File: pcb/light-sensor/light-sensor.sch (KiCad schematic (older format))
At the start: 13 parts, among them J1 HEADER-1x04, J2 HEADER-1x01, Q1 BSS138, Q2 BSS138, U1 LP2981, U2 TSL2561

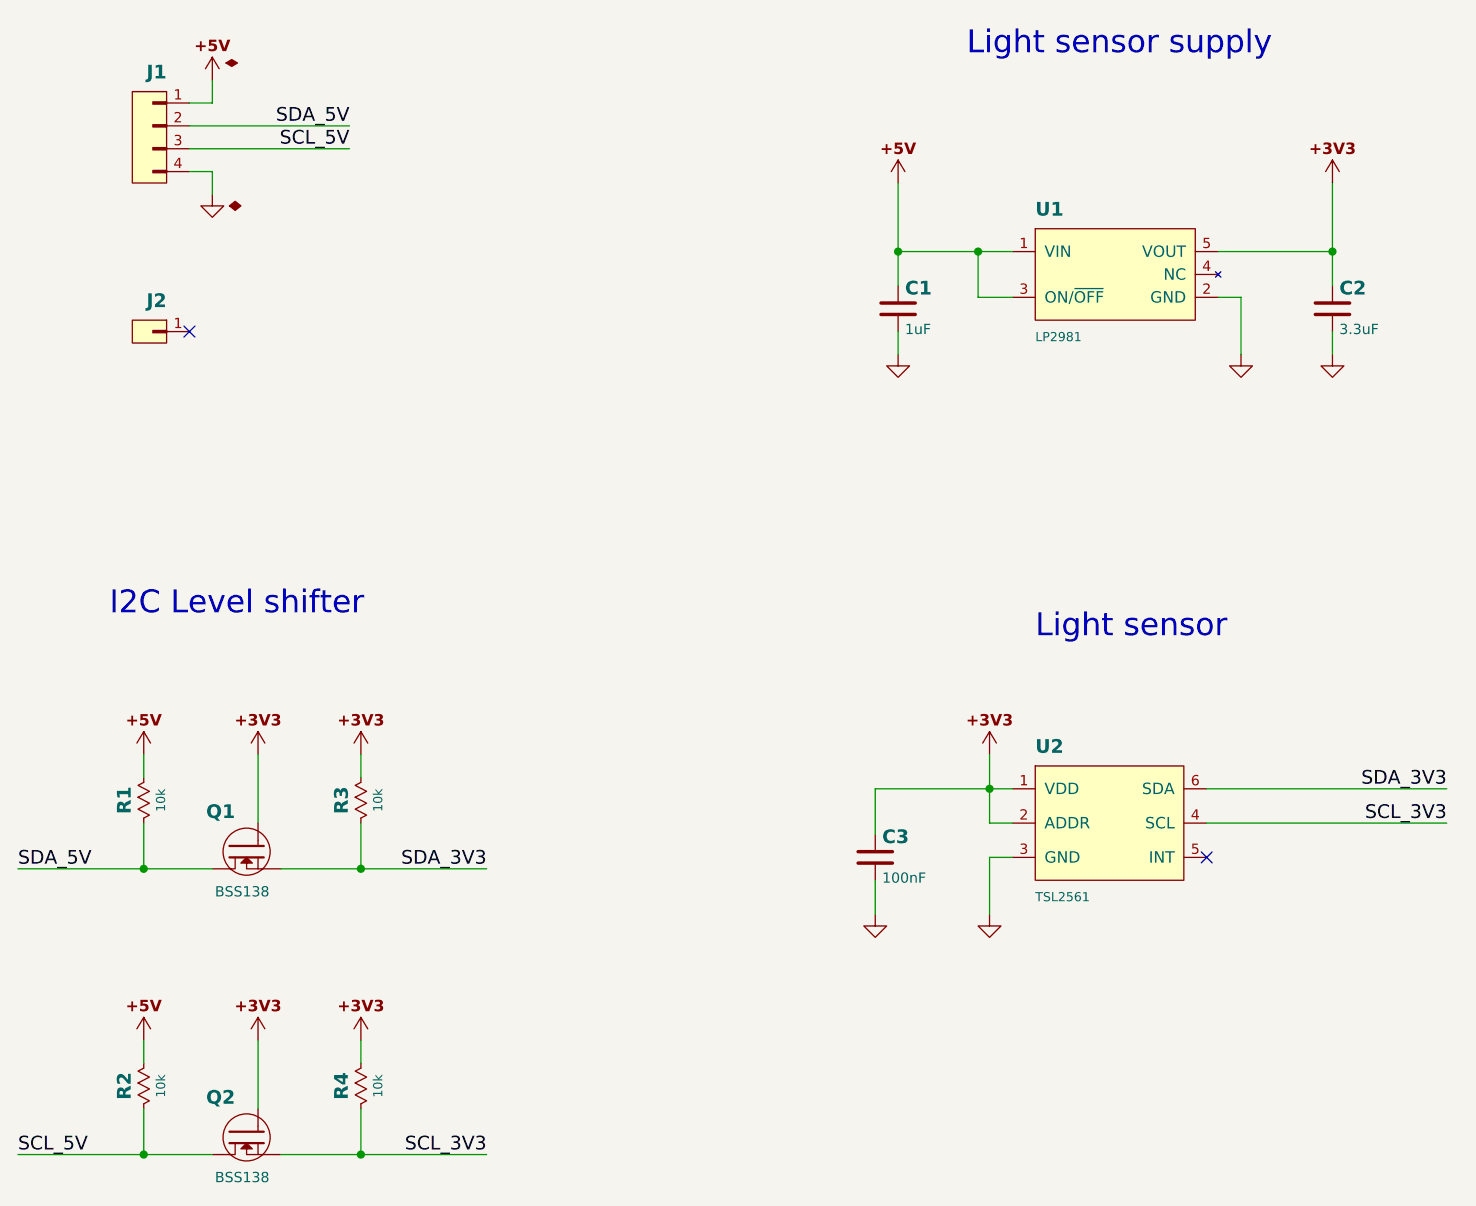
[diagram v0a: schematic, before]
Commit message: Removed 3.3v regulator and level shifters
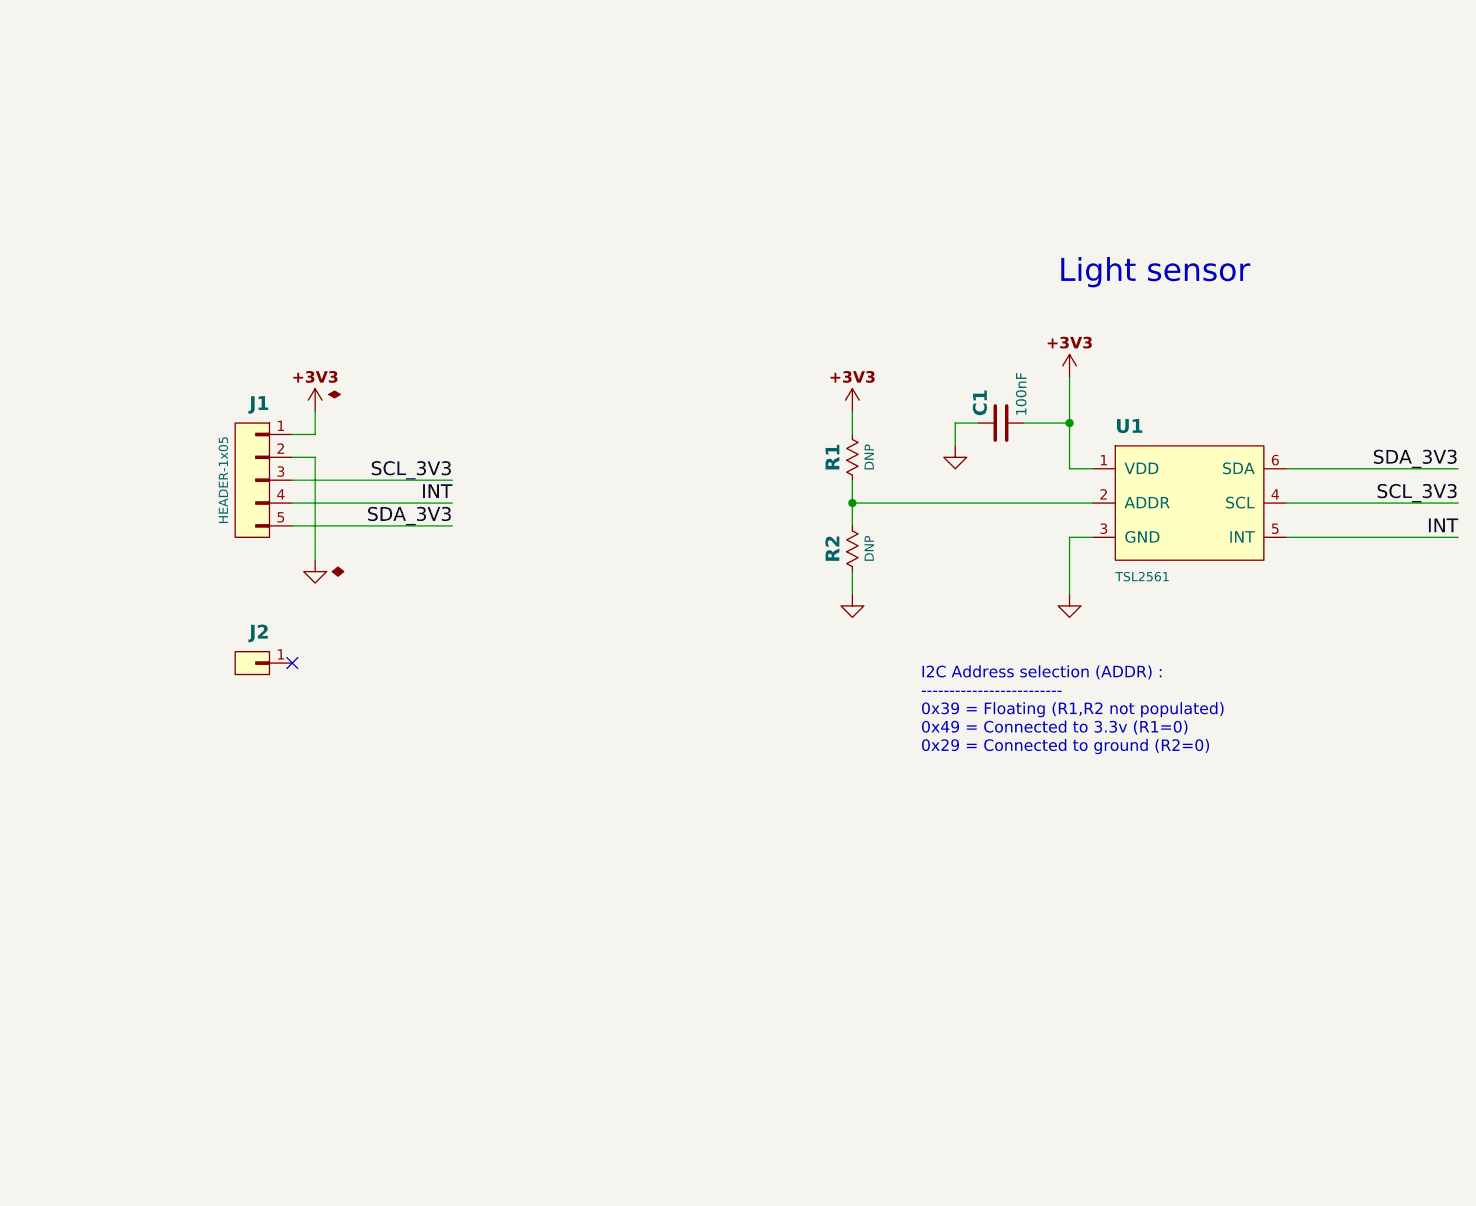
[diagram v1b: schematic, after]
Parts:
- removed C1: 1uF, SMT:C-0805, symbol CAP
- removed C2: 3.3uF, SMT:C-0805, symbol CAP
- removed J1: HEADER-1x04, Conn-Wire-Pads:WP-50mil-1x04, symbol HEADER-1x04
- removed Q1, Q2: BSS138, SMT-SOT:SOT23, symbol N-MOSFET
- removed R3, R4: 10k, SMT:R-0603, symbol RESISTOR
- removed U1: LP2981, SMT-SOT:SOT23-5, symbol LP2981
- added J1: HEADER-1x05, Conn-Wire-Pads:WP-40mil-1x05, symbol HEADER-1x05
- J2: footprint Conn-Wire-Pads:SolderPad-100x300 -> Conn-Wire-Pads:SolderPad-100x150
- R1, R2: value 10k -> DNP
- renumbered C3 to C1, U2 to U1
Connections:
- net SCL_5V is gone; now on an unnamed net: R2.2
- net SDA_5V is gone; now on net +3V3: R1.2
- net +3V3: now also C1.1, J1.1 (P1); no longer C1.2, U1.2 (ADDR)
- net GND: now also C1.2, R2.1, J1.2 (P2); no longer C1.1
- net SCL_3V3: now also J1.3 (P3)
- net SDA_3V3: now also J1.5 (P5)
- net INT: now reaches U1.5 (INT)
- net INT: now also J1.4 (P4)
- net +5V: no longer names the net of R1.1
- net +5V: now also U1.2 (ADDR); no longer R2.1
- no-connect marks 2 -> 1
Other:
- note added: "I2C Address selection (ADDR) :\n-------------------------\n0x39 = Floating (R1,R2 not populated)\n0x49 = Connected to 3.3v (R1=0)\n0x29 = Connected to ground (R2=0)"
- note removed: "I2C Level shifter"
- note removed: "Light sensor supply"
- moved on the sheet: C1, J2, U1
